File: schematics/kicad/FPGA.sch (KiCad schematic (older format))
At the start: 3 parts, among them U8 XC6SLXN-TQG144

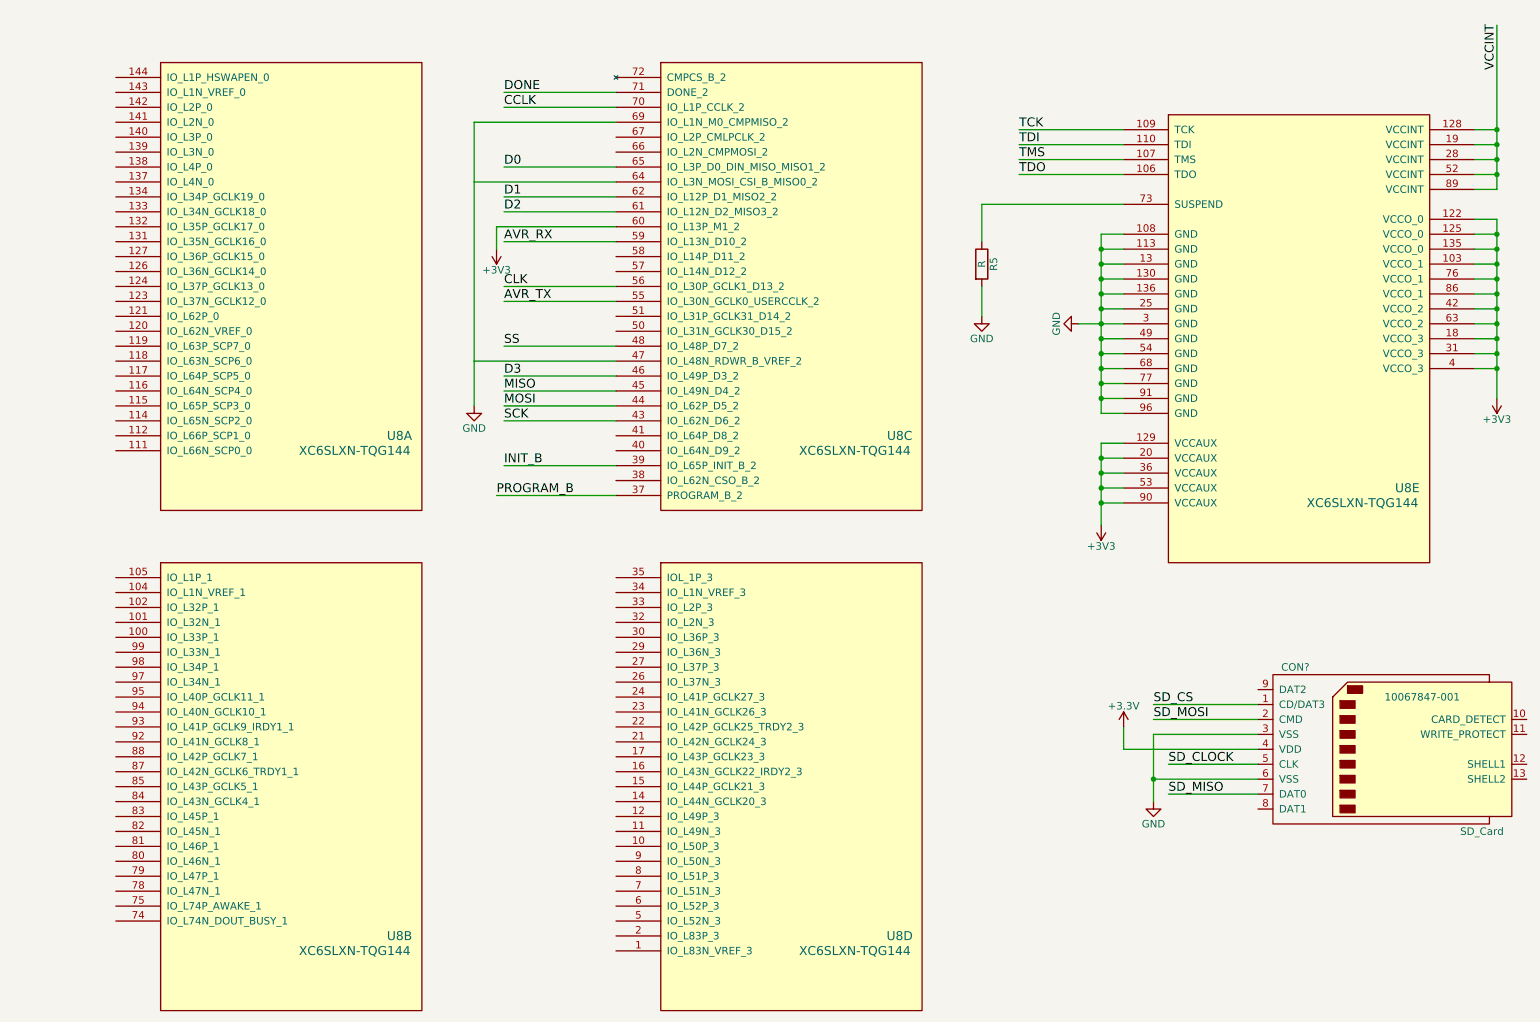
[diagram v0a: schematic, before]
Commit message: Change a lot of things, especially pinning between sheets
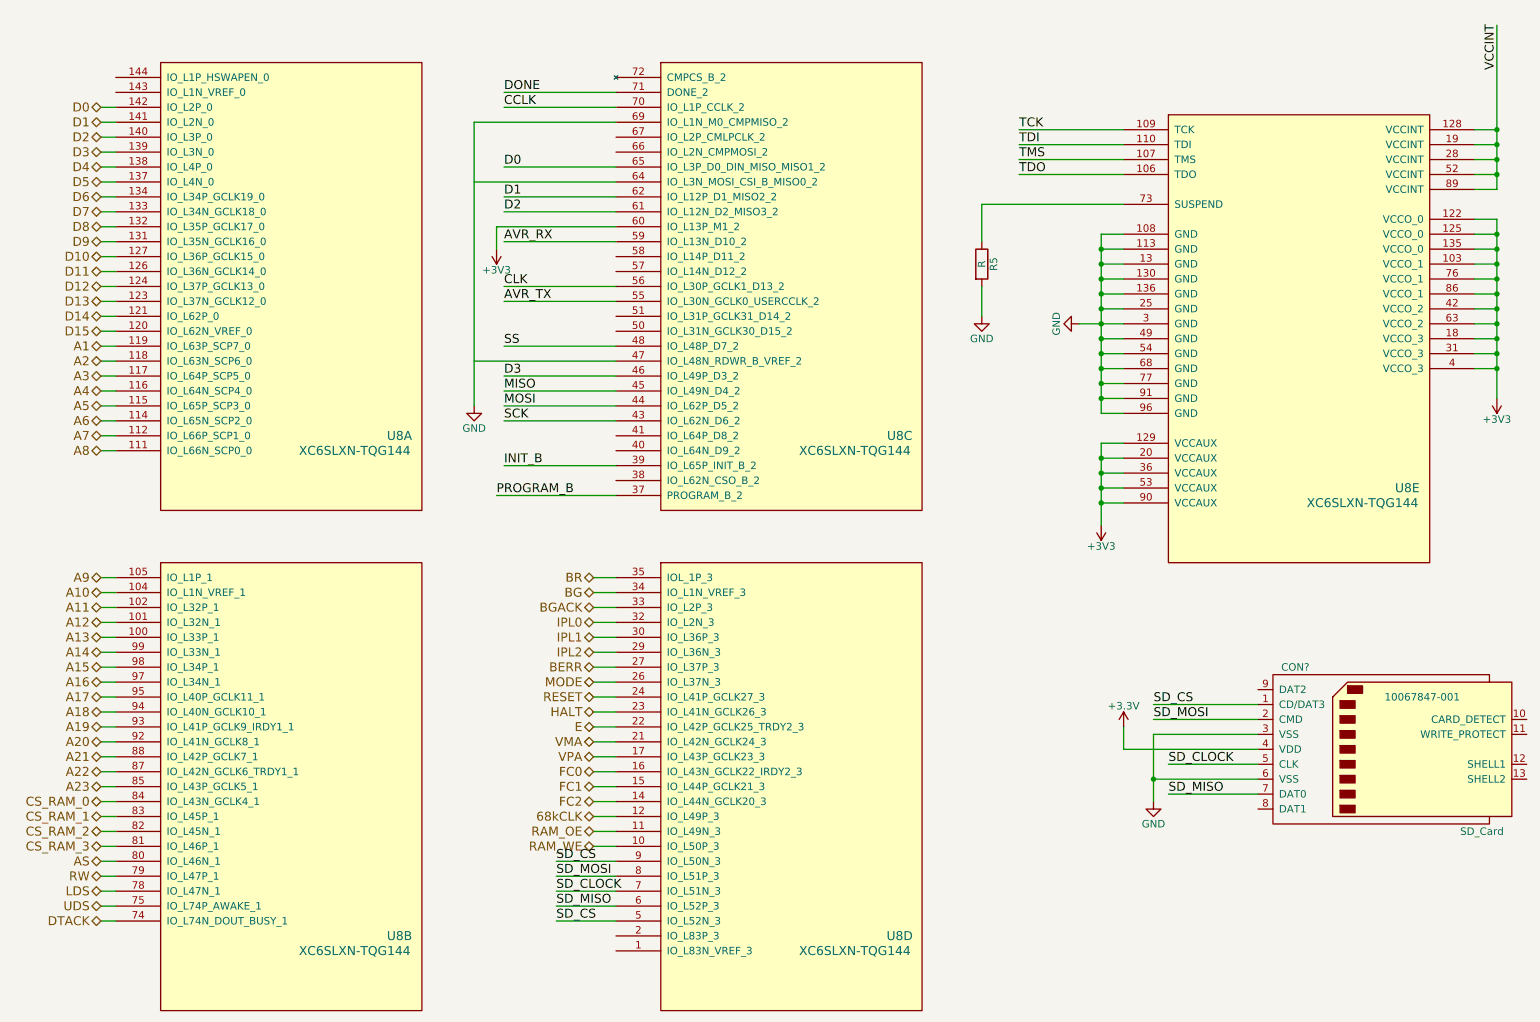
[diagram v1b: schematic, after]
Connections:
- net labels added: 68kCLK, A1, A10, A11, A12, A13, A14, A15, A16, A17, A18, A19, A2, A20, A21, A22, A23, A3, A4, A5, A6, A7, A8, A9, AS, BERR, BG, BGACK, BR, CS_RAM_0, CS_RAM_1, CS_RAM_2, CS_RAM_3, D10, D11, D12, D13, D14, D15, D4, D5, D6, D7, D8, D9, DTACK, E, FC0, FC1, FC2, HALT, IPL0, IPL1, IPL2, LDS, MODE, RAM_OE, RAM_WE, RESET, RW, UDS, VMA, VPA
- wire segments 75 -> 147
